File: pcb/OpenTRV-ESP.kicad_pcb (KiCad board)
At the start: 4 copper layers, 45 x 53 mm, 64 parts, among them J1 TagConnect_TC2030, J2 I2C, J3 Buttons, J4 Screen, J5 Stepper Motor, P1 USB_C_Plug_USB2.0, Q1 FDN340P, Q2 BSS123, Q3 BSS123, SW1 EN Push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

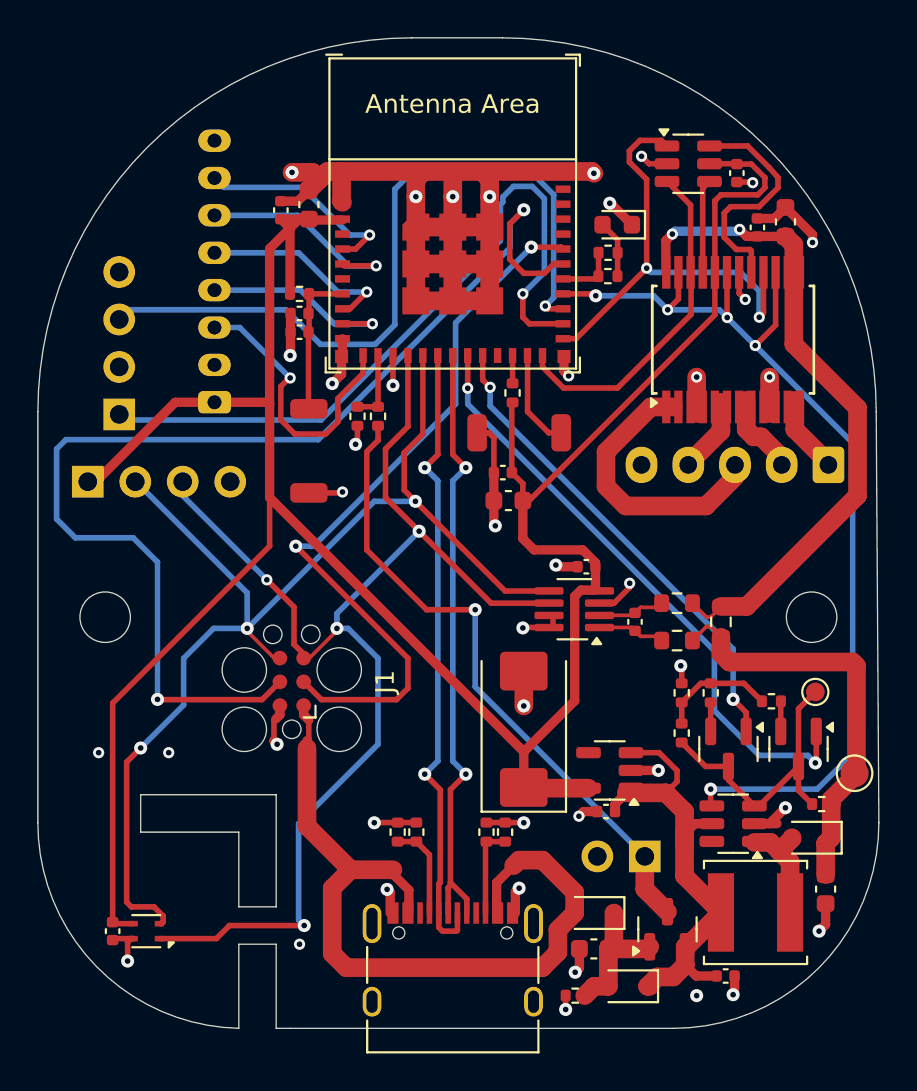
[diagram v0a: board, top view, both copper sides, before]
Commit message: Reconnects the stepper driver to the ESP ULP pins
Redoes the board layout and routing.
The temperature sensor is now centered at the bottom of the board.
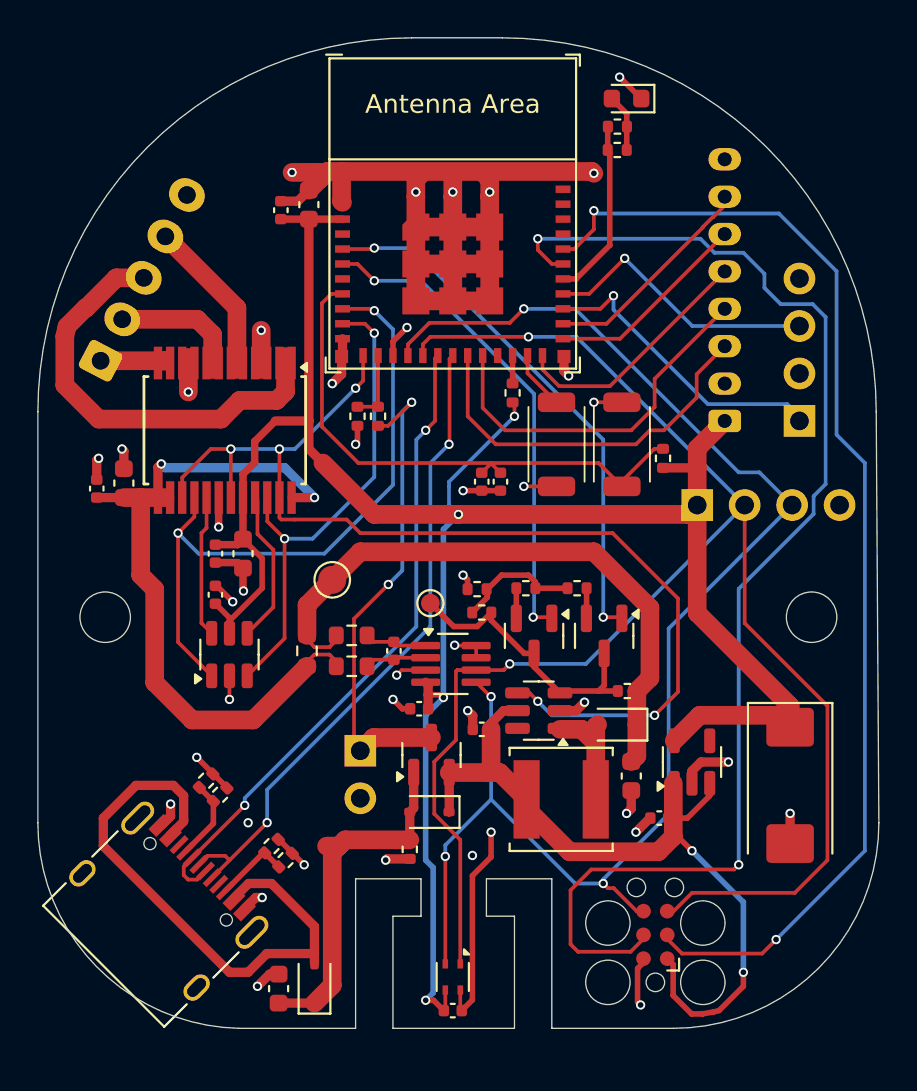
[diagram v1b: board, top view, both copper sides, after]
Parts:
- TP2: value V_FB -> V_SM
- moved J5 39.3 mm to (47.4, 62.3), turned to 62.5 degrees
- moved C15 38.1 mm to (48.6, 68.8)
- moved C16 38.0 mm to (47.1, 69.1)
- moved J3 36.4 mm to (84.8, 65.5)
- moved U5 36.0 mm to (54.2, 78.0), turned to 90 degrees
- moved C10 35.9 mm to (53.5, 74.8), turned to 90 degrees
- moved J2 32.6 mm to (79.3, 70.0)
- moved TP1 29.8 mm to (59.8, 74.0), turned to 0 degrees
- moved U6 27.6 mm to (54.0, 66.0), turned to -90 degrees
- moved J4 27.3 mm to (80.8, 65.5)
- moved J1 23.7 mm to (77.0, 93.0)
- moved R18 22.2 mm to (58.4, 77.8), turned to -90 degrees
- moved R3 21.3 mm to (77.5, 67.5), turned to 90 degrees
- moved TP2 21.1 mm to (65.0, 75.2), turned to 0 degrees
- moved C1 18.7 mm to (66.2, 97.0), turned to 0 degrees
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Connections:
- J1 pad 1: /VIN_5V -> /VIN_LS
- J2 pad 2: /SCL -> /SDA
- J2 pad 3: /SDA -> /SCL
- U3 pad 10: /CLK -> /DIR1
- U3 pad 12: /DIN -> /EN_SM
- U3 pad 15: /SDA -> /SCL
- U3 pad 16: /SCL -> /SDA
- U3 pad 19: /SEL_9V_VMS -> /DIN
- U3 pad 20: /SEL_12V_VMS -> /CLK
- U3 pad 24: /DIR1 -> /CS
- U3 pad 25: /DIR2 -> /DC
- U3 pad 26: /BTN1 -> /RST
- U3 pad 27: /BTN2 -> /BTN1
- U3 pad 28: /EN_SM -> /BTN2
- U3 pad 5: /RST -> /SEL_9V_VMS
- U3 pad 6: /DC -> /SEL_12V_VMS
- U3 pad 9: /CS -> /DIR2
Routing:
- net /BTN2: track 39.9 -> 15.2 mm
- net /TXD: track 39.8 -> 62.2 mm
- net /BTN1: track 38.7 -> 16.4 mm
- net Net-(U3-EN/CHIP_PU): track 7.92 -> 29.6 mm
- net /SDA: track 67.5 -> 88.2 mm, vias 4 -> 2
- net /VIN_LS: track 26.1 -> 43.2 mm, vias 0 -> 2
- net +3.3V: track 137.6 -> 122.7 mm, vias 0 -> 4
- net /SCL: track 63.6 -> 77.8 mm, vias 3 -> 4
- net /VIN_5V: track 42.8 -> 31.2 mm
- net +5V: track 7.77 -> 19.1 mm
- net Net-(D4-K): track 22.3 -> 32.9 mm
- net /DIR2: track 25.5 -> 35.6 mm
- net /CLK: track 10.8 -> 19.8 mm, vias 1 -> 0
- net Net-(J5-Pin_3): track 14.4 -> 23.4 mm
- net /DIR1: track 18.3 -> 26.5 mm, vias 0 -> 2
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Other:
- outline, holes or cut-outs redrawn

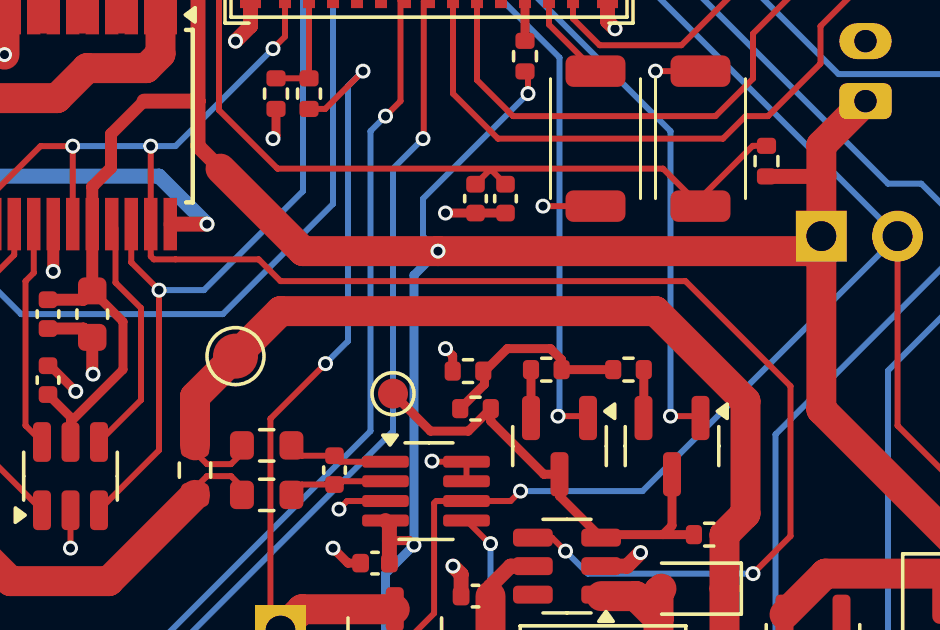
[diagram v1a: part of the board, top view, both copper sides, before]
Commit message: Improves the M30 mounting nut
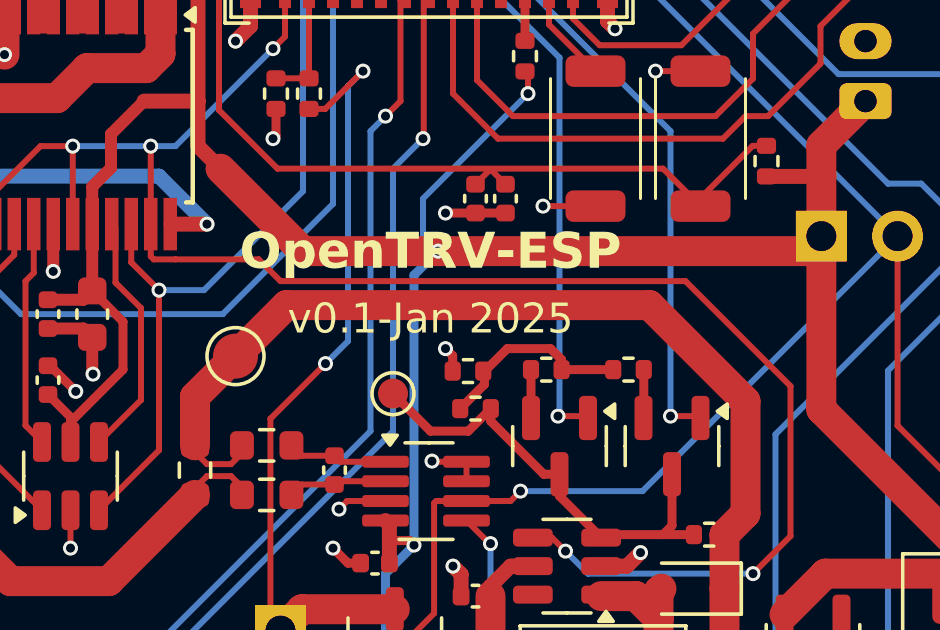
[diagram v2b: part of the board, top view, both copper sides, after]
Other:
- board text added: "@mpiraux"
- board text added: "OpenTRV-ESP"
- board text added: "v0.1-Jan 2025"

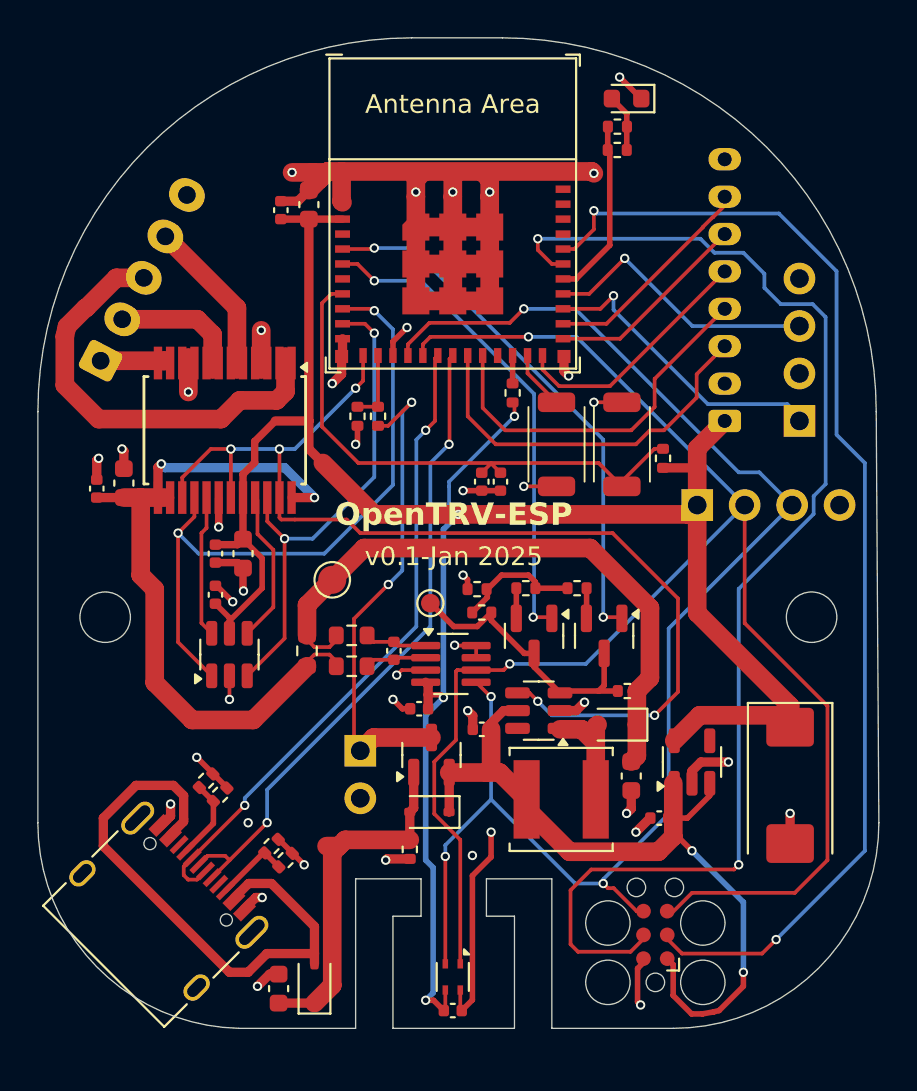
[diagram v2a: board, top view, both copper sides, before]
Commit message: WIP TMC2300
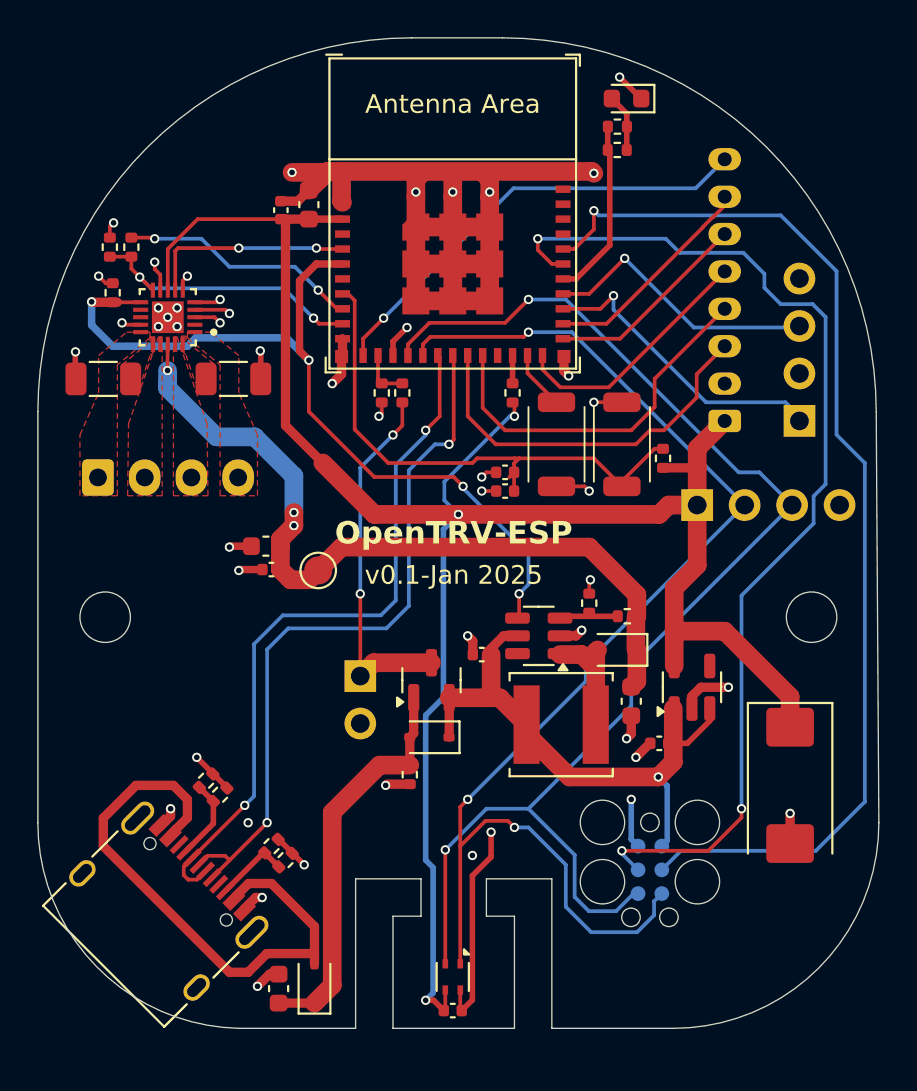
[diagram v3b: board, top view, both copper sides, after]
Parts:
- removed C10, C12, C17, C18: 100n, Capacitor_SMD:C_0402_1005Metric
- removed C11: 10µ, Capacitor_SMD:C_0603_1608Metric
- removed Q2, Q3: BSS123, Package_TO_SOT_SMD:SOT-23
- removed R14, R15: 180k, Resistor_SMD:R_0402_1005Metric
- removed R16: 10k, Resistor_SMD:R_0402_1005Metric
- removed R19: 100R, Resistor_SMD:R_0603_1608Metric
- removed TP2: V_SM, TestPoint:TestPoint_Pad_D1.0mm
- removed U5: SN74LVC2G14DBV, Package_TO_SOT_SMD:SOT-23-6
- removed U6: TB6612FNG, Package_SO:SSOP-24_5.3x8.2mm_P0.65mm
- removed U7: INA219AxDCN, Package_TO_SOT_SMD:SOT-23-8_Handsoldering
- added R20: 330m Low I, Resistor_SMD:R_1206_3216Metric, F.Cu at (47.5, 63.3)
- added R21: 330m Low I, Resistor_SMD:R_1206_3216Metric, F.Cu at (54.5, 63.2)
- added R22: 10k, Resistor_SMD:R_0402_1005Metric, F.Cu at (48.0, 58.6)
- added U8: TMC2300-LA-T, mpiraux:QFN40P300X300X90-21N, F.Cu at (51.0, 60.0)
- J1: moved to B.Cu
- J5: footprint Connector_JST:JST_XH_B5B-XH-A_1x05_P2.50mm_Vertical -> Connector_JST:JST_XH_B4B-XH-A_1x04_P2.50mm_Vertical
- R13: value 180k -> 86k6
- R17: value 100R -> 1M; footprint Resistor_SMD:R_0603_1608Metric -> Resistor_SMD:R_0402_1005Metric
- R18: value 20m -> 10k; footprint Resistor_SMD:R_0603_1608Metric -> Resistor_SMD:R_0402_1005Metric
- moved R17 24.5 mm to (47.9, 56.2), turned to -90 degrees
- moved R18 23.6 mm to (49.0, 56.2)
- moved C16 10.3 mm to (56.5, 73.5), turned to 180 degrees
- moved C15 8.32 mm to (56.2, 72.2), turned to 180 degrees
- moved J5 6.25 mm to (47.2, 68.5), turned to 0 degrees
- moved BT1 4.00 mm to (61.2, 79.2)
- moved C13 4.00 mm to (75.8, 80.5)
- moved C2 4.00 mm to (77.2, 82.8)
- moved C8 4.00 mm to (67.8, 78.0)
- moved D1 4.00 mm to (65.0, 82.4)
- moved D4 4.00 mm to (75.0, 77.8)
- moved L1 4.00 mm to (72.0, 81.8)
- moved Q1 4.00 mm to (65.1, 79.4)
- moved R12 4.00 mm to (75.5, 76.0)
- moved R4 4.00 mm to (63.9, 84.4)
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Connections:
- C13 pad 1: Net-(D4-K) -> /V_SM
- D4 pad 1: Net-(D4-K) -> /V_SM
- J5 pad 1: Net-(J5-Pin_1) -> /B2
- J5 pad 2: Net-(J5-Pin_2) -> /B1
- J5 pad 3: Net-(J5-Pin_3) -> /A1
- J5 pad 4: Net-(J5-Pin_4) -> /A2
- R12 pad 1: Net-(Q2-D) -> Net-(U4-FB)
- R12 pad 2: Net-(D4-K) -> /V_SM
- R13 pad 1: Net-(R13-Pad1) -> GND
- R13 pad 2: Net-(Q2-S) -> Net-(U4-FB)
- R17 pad 1: Net-(U7-IN+) -> GND
- R17 pad 2: Net-(D4-K) -> /DRV_UART_RX
- R18 pad 1: Net-(D4-K) -> /DRV_UART_TX
- R18 pad 2: /V_SM -> /DRV_UART_RX
- TP1 pad 1: Net-(D4-K) -> /V_SM
- U3 pad 10: /DIR1 -> /DRV_UART_RX
- U3 pad 12: /EN_SM -> /BUSY
- U3 pad 5: /SEL_9V_VMS -> /EN_DRV
- U3 pad 6: /SEL_12V_VMS -> /EN_SM
- U3 pad 9: /DIR2 -> /DRV_UART_TX
- U4 pad 3: Net-(Q2-D) -> Net-(U4-FB)
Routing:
- net /DIR2: track 35.6 -> 0.00 mm, vias 2 -> 0
- net Net-(D4-K): track 33.1 -> 0.00 mm
- net /SEL_9V_VMS: track 28.7 -> 0.00 mm, vias 2 -> 0
- net /DIR1: track 26.5 -> 0.00 mm, vias 2 -> 0
- net /SEL_12V_VMS: track 26.1 -> 0.00 mm, vias 2 -> 0
- net /BUSY: track 0.00 -> 24.2 mm, vias 0 -> 1
- net Net-(J5-Pin_3): track 23.4 -> 0.00 mm
- net /SDA: track 88.2 -> 69.2 mm, vias 2 -> 3
- net Net-(Q2-D): track 15.3 -> 0.00 mm
- net /DRV_UART_RX: track 0.00 -> 15.3 mm, vias 0 -> 2
- net /EN_SM: track 58.3 -> 45.2 mm, vias 5 -> 4
- net /DRV_UART_TX: track 0.00 -> 12.9 mm, vias 0 -> 2
- net /VIN_LS: track 43.2 -> 30.4 mm, vias 2 -> 1
- net +3.3V: track 122.7 -> 111.2 mm, vias 4 -> 3
- net /EN_DRV: track 0.00 -> 11.1 mm, vias 0 -> 2
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- added copper zone on F.Cu, net /A1
- added copper zone on F.Cu, net /A2
- added copper zone on F.Cu, net /B1
- added copper zone on F.Cu, net /B2
- added copper zone on F.Cu, net Net-(U8-BRA)
- added copper zone on F.Cu, net Net-(U8-BRB)
